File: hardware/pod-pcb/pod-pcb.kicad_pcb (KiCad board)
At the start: 4 copper layers, 50 x 94 mm, 4 parts

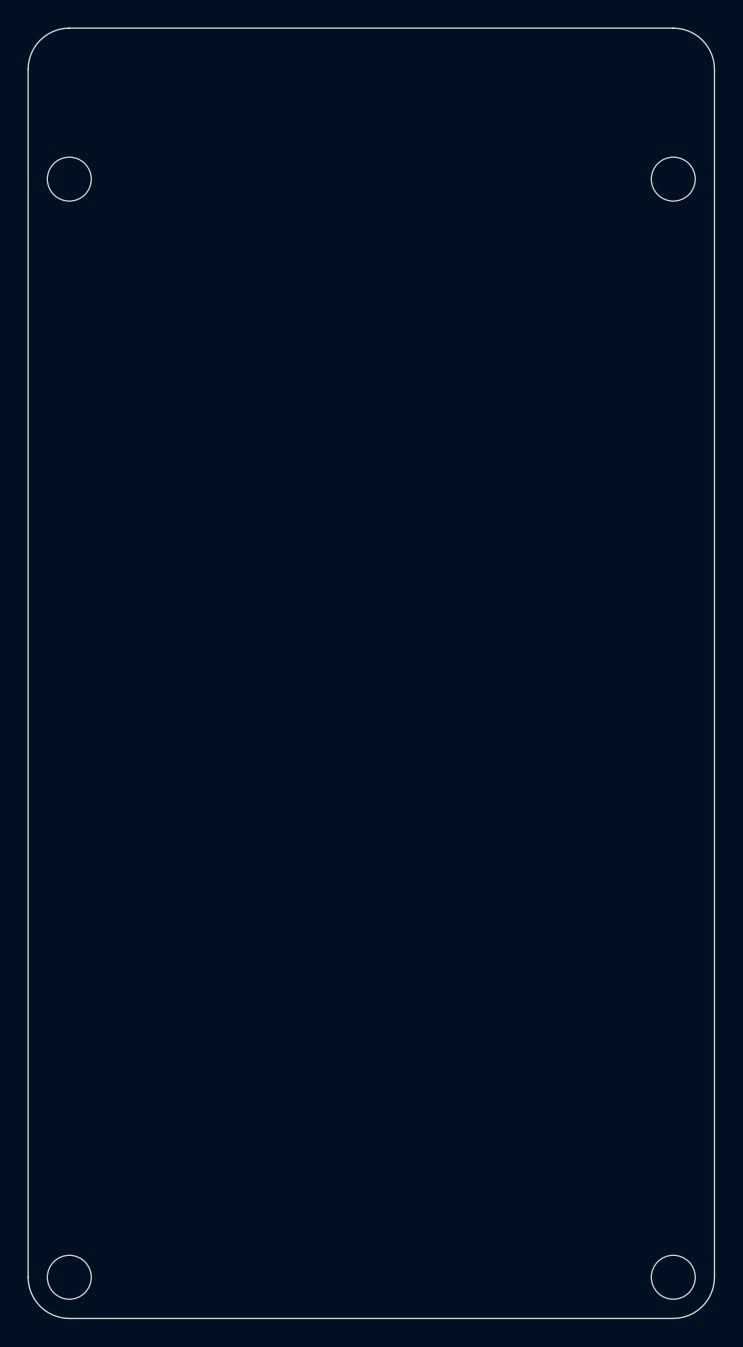
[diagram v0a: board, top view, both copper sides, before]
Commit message: PCB: place screen module holes and headers from measurements
- Module positions measured from a photo of the MSP2807 V1.2 module:
  M2.5 holes, J3 14-pin and J4 4-pin SD header positions, and the SD
  card holder, mirrored onto our board (module faces down onto it)
- Pin markers, pin-1 marks, SD holder keep-clear area and a 50 mm
  scale bar on the board drawing layer
- docs/screen_template_1to1.pdf: printable 1:1 check template
- hardware/pod-pcb/generate_skeleton.py: script that generated the
  starting project (kept for reference)

Co-Authored-By: Claude Opus 5.5 <noreply@anthropic.com>
Claude-Session: https://claude.ai/code/session_01DRxt8QzQ72ypvJY6iWLH7J
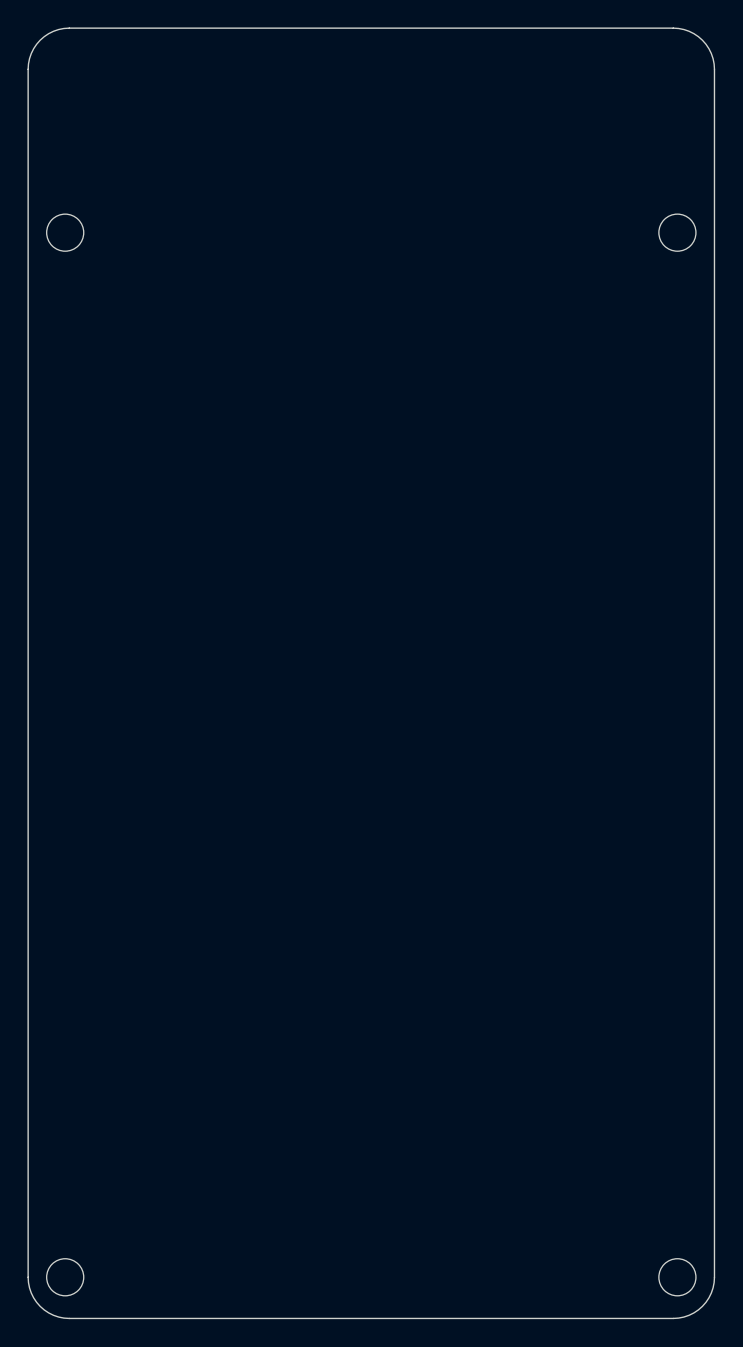
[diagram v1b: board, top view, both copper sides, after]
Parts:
- H1, H2, H3, H4: value M3 (module hole - verify position) -> M2.5 module hole; footprint MountingHole:MountingHole_3.2mm_M3 -> MountingHole:MountingHole_2.7mm_M2.5
- moved H1 44.5 mm to (147.3, 64.9)
- moved H2 44.5 mm to (102.7, 64.9)
- moved H3 44.3 mm to (147.3, 141.0)
- moved H4 44.3 mm to (102.7, 141.0)
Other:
- board text added: "2.8" module MSP2807 V1.2, 50 x 86 mm (from photo: verify with the print template)"
- board text added: "<- SW1, SW2 on this edge"
- board text added: "J3 pin 1 VCC"
- board text added: "J4 pin 1 SD_CS"
- board text added: "USB-C"
- board text added: "card enters from this edge ->"
- board text added: "jack"
- board text added: "module SD holder above: keep clear"
- board text added: "this bar must measure exactly 50 mm on paper"
- board text removed: "2.8" screen module 50 x 86 mm (MEASURE YOURS)"
- board text removed: "Battery 503450 (34 x 50 x 5) in the socket gap"
- board text removed: "J3 14-pin socket (position: measure)"
- board text removed: "J4 4-pin SD socket (position: measure)"
- board text removed: "SW1 SW2 ->"
- board text removed: "USB-C jack (bottom edge)"
- board text removed: "keep clear under the module microSD slot"

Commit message: PCB: battery moves to the underside of the board
The screen module's microSD holder occupies the gap under the module,
so the 1000 mAh cell no longer fits beside it. It now sits on the
underside of our board (one-sided assembly, no parts on the bottom),
with its lead through a notch to J2. Pod is about 55 x 100 x 24 mm.
Layout, case and progress notes updated; battery outline on B.Fab.

Co-Authored-By: Claude Opus 5.5 <noreply@anthropic.com>
Claude-Session: https://claude.ai/code/session_01DRxt8QzQ72ypvJY6iWLH7J
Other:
- board text added: "J2 + lead notch"
- board text added: "UNDERSIDE: battery 503450 (34 x 50 x 5), foam tape"
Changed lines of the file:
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@@
+    (effects (font (size 0.7 0.7) (thickness 0.15)) (justify left))
+  )
+  (gr_rect (start 108.0 76.0) (end 142.0 126.0) (stroke (width 0.12) (type default)) (fill none) (layer "B.Fab"))
+  (gr_text "UNDERSIDE: battery 503450 (34 x 50 x 5), foam tape" (at 109.0 79.0) (layer "B.Fab")
+    (effects (font (size 0.8 0.8) (thickness 0.15)) (justify left))
+  )
+  (gr_text "J2 + lead notch" (at 101.0 118.0) (layer "Cmts.User")
     (effects (font (size 0.7 0.7) (thickness 0.15)) (justify left))
   )
